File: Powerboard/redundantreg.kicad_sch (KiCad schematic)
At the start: 34 parts, among them Q10 MCH6351, Q9 MCH6351, U6 LM2679T-3.3-iclr, U7 LM2679T-3.3-iclr, U8 LTC4412xS6, U9 LTC4412xS6

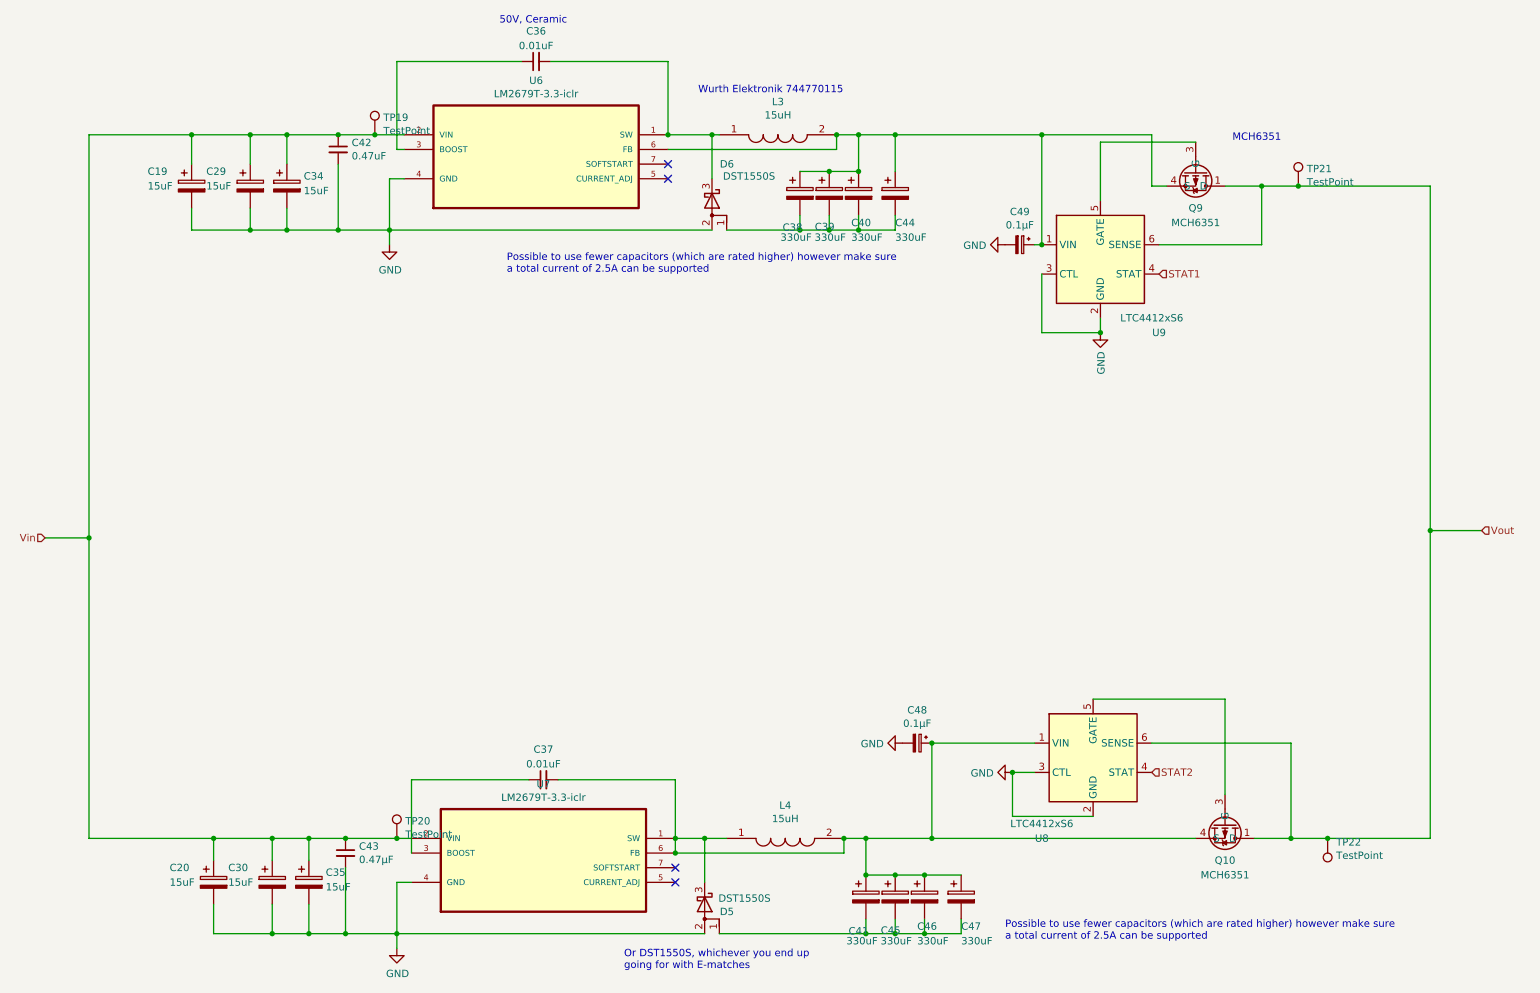
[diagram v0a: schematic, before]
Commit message: Finalised buck capacitors, some inital layout
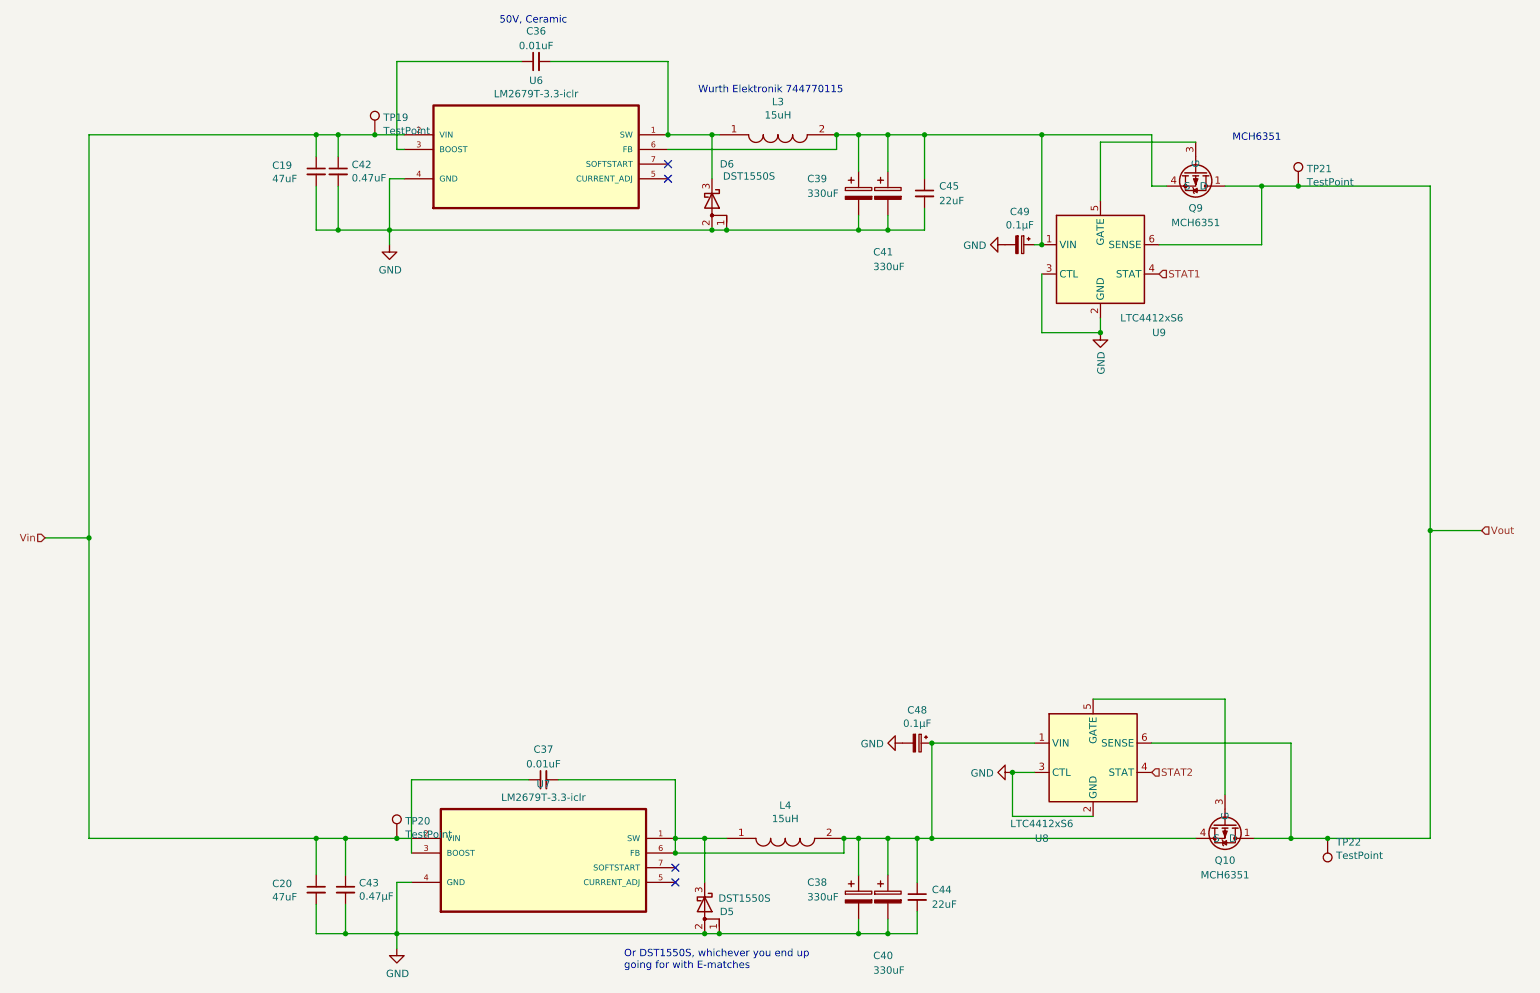
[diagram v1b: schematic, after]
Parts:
- removed C19, C20, C29, C30, C34, C35: 15uF, Capacitor_SMD:CP_Elec_5x5.3, symbol Device:C_Polarized
- removed C44, C45, C46, C47: 330uF, Capacitor_SMD:CP_Elec_10x10, symbol Device:C_Polarized
- added C19, C20: 47uF, Capacitor_SMD:C_2220_5650Metric, symbol Device:C_Small
- added C44, C45: 22uF, Capacitor_SMD:C_0603_1608Metric, symbol Device:C_Small
- C38, C39, C40, C41: footprint Capacitor_SMD:CP_Elec_10x10 -> Capacitor_Tantalum_SMD:CP_EIA-7343-30_AVX-N
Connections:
- net GND: now also C38.2, C39.2, C40.2, C41.2, D5.1 (A), D6.1 (A), C19.2, C20.2, C44.2, C45.2
- net Vin: now also C19.1, C20.1
- net at C37.2, C48.1, D5.3 (K)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: now also C38.1, C40.1, C44.1; no longer C41.1
- net at C39.1, C49.1, L3.2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: now also C41.1, C45.1; no longer C38.1, C40.1
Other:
- note removed: "Possible to use fewer capacitors (which are rated higher) however make sure a total current of 2.5A can be supported"
- moved on the sheet: C42, C43

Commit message: layout
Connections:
- net at C38.1, C40.1, C44.1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: no longer C37.2, D5.3 (K), L4.1, U7.1 (SW)
- new net: C37.2, D5.3 (K), L4.1, U7.1 (SW)
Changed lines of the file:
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@@
   (junction (at 163.83 41.91) (diameter 0) (color 0 0 0 0)
-  )
-  (junction (at 127 149.86) (diameter 0) (color 0 0 0 0)
   )
   (junction (at 135.89 41.91) (diameter 0) (color 0 0 0 0)
@@
     (stroke (width 0) (type default) (color 0 0 0 0))
   )
-  (wire (pts (xy 127 147.32) (xy 127 149.86))
-    (stroke (width 0) (type default) (color 0 0 0 0))
-  )
